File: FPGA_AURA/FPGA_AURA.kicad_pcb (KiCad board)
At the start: 10 copper layers, 50 x 50 mm, 161 parts, among them J1 SS5-40-3.00-X-D-K-XX, J2 SS5-20-3.00-X-D-K-XX, U1 XC7A35T-2FTG256C, U2 W25Q256JVEIQ, U200 ADP5014, U4 TPS51200DRCR, U500 MT41K128M16JT-125_IT_K

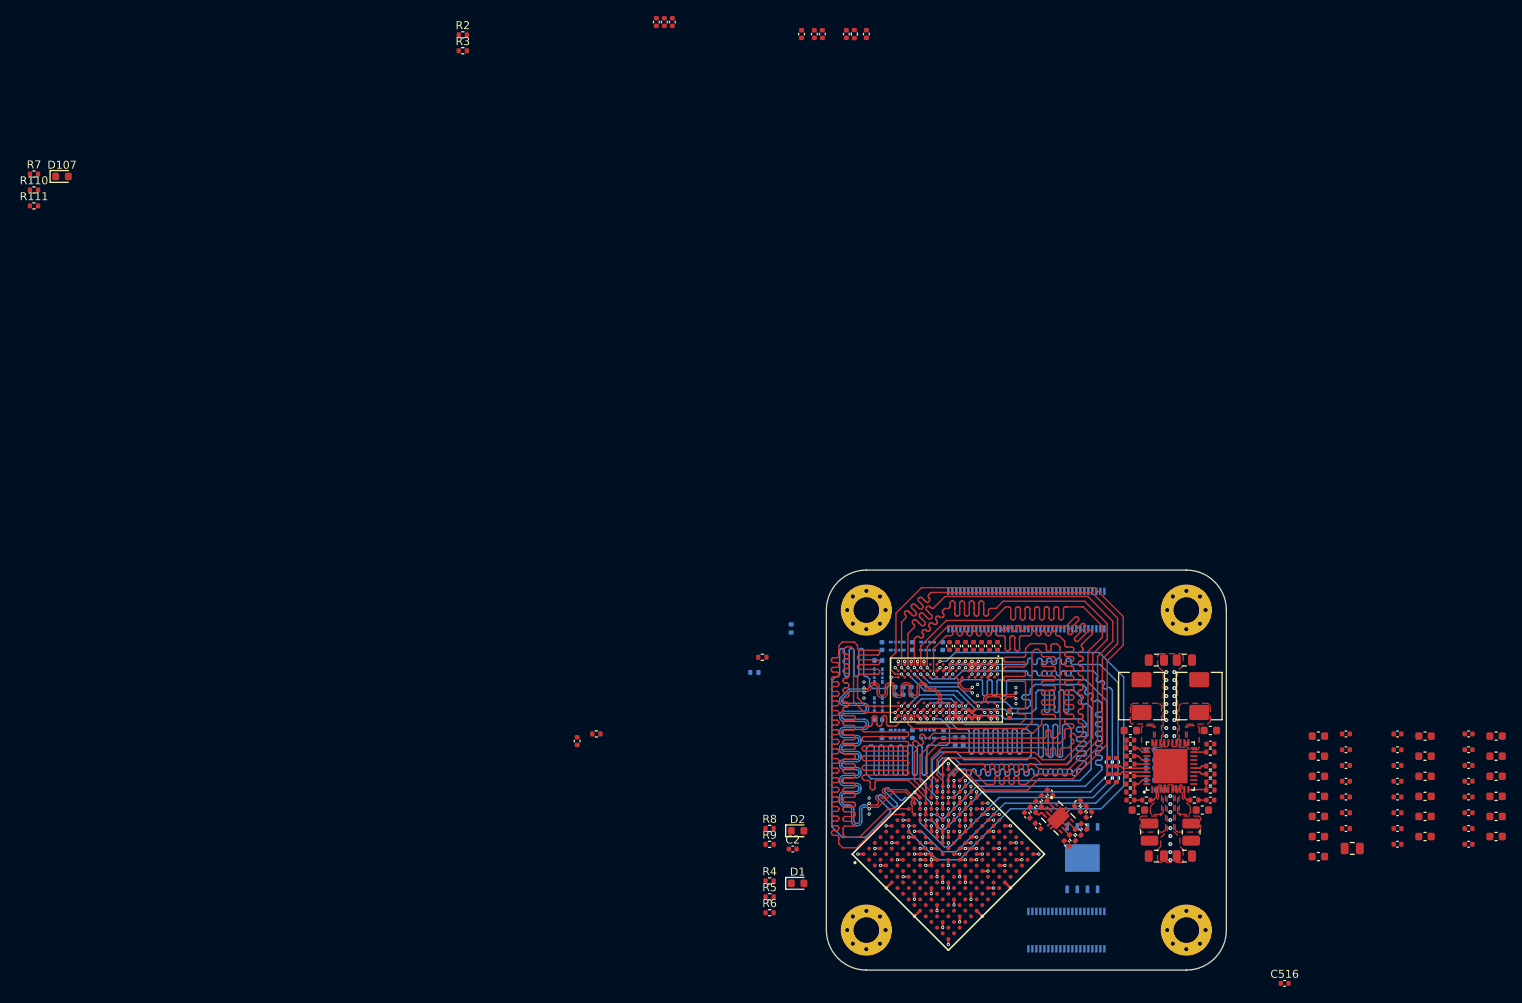
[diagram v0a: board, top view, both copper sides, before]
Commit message: Finished schematic to start routing again, and started MII fanout from connector.
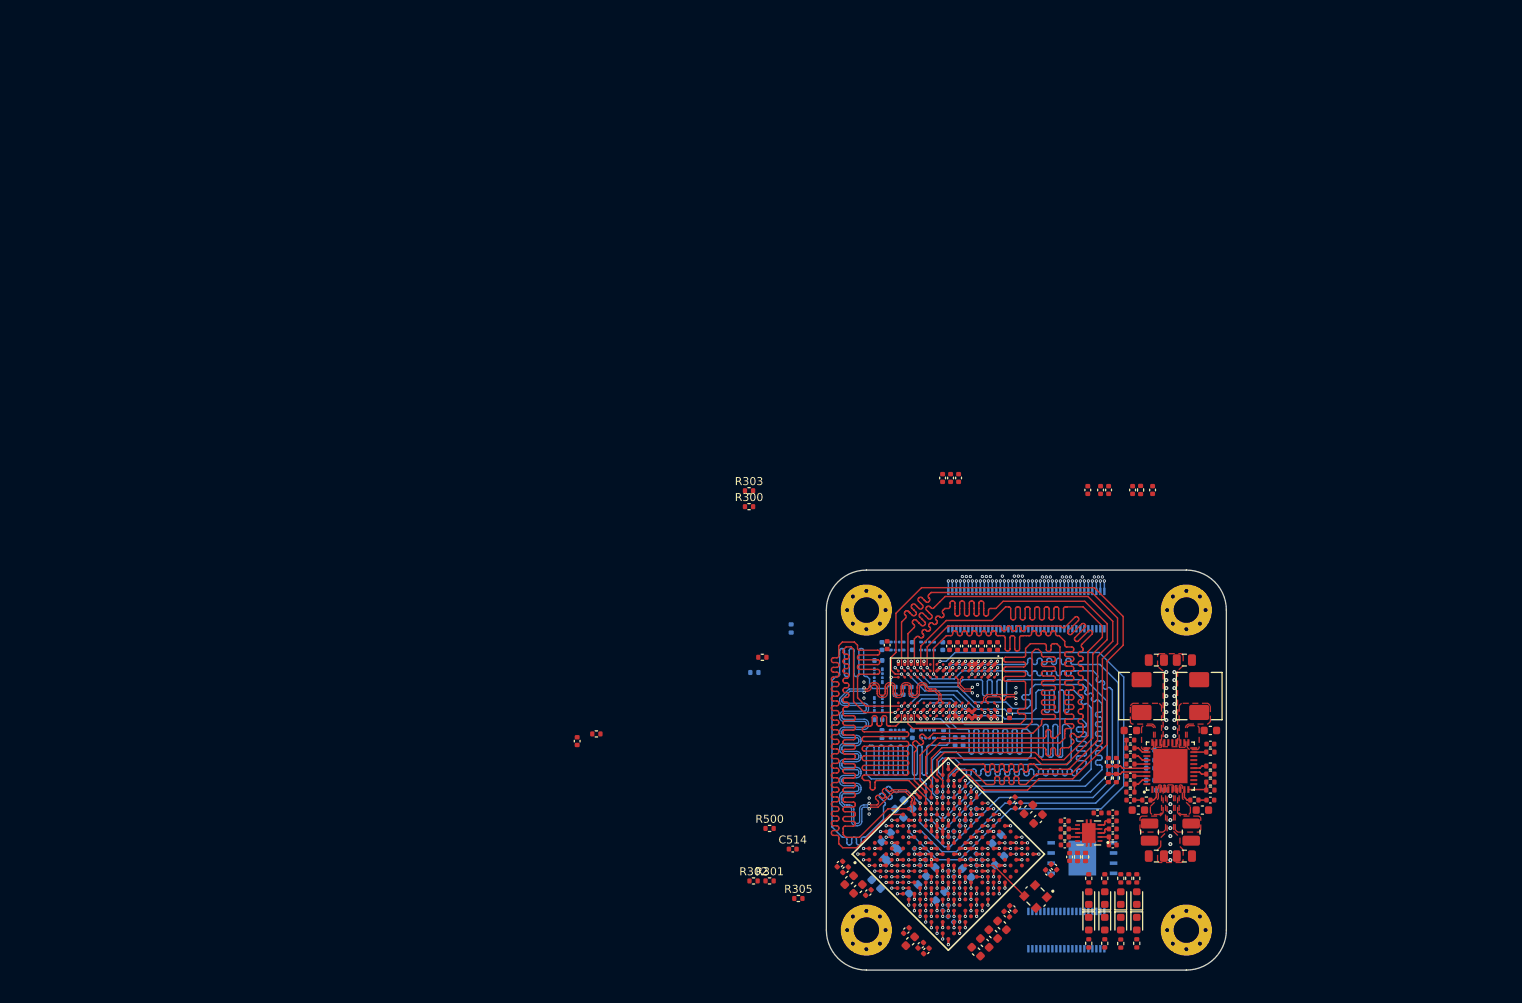
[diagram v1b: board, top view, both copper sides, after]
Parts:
- added D1: LED, LED_SMD:LED_0603_1608Metric, F.Cu at (138.8, 91.0)
- added D700: LED, LED_SMD:LED_0603_1608Metric, F.Cu at (132.8, 94.2)
- added D701: LED, LED_SMD:LED_0603_1608Metric, F.Cu at (134.8, 94.2)
- added D702: LED, LED_SMD:LED_0603_1608Metric, F.Cu at (136.8, 94.2)
- added D703: LED, LED_SMD:LED_0603_1608Metric, F.Cu at (138.8, 94.2)
- added R502: 470R, Resistor_SMD:R_0402_1005Metric, F.Cu at (138.8, 88.5)
- added R700: 27R, Resistor_SMD:R_0402_1005Metric, F.Cu at (132.8, 96.7)
- added R701: 120R, Resistor_SMD:R_0402_1005Metric, F.Cu at (134.8, 96.7)
- added R702: 80R, Resistor_SMD:R_0402_1005Metric, F.Cu at (136.8, 96.7)
- added R704: 470R, Resistor_SMD:R_0402_1005Metric, F.Cu at (138.8, 96.7)
- added Y500: ASEM1-100.000MHZ-LC-T, ASEM1-100.000MHZ-LC-T:XTAL_ASEM1-100.000MHZ-LC-T, F.Cu at (126.2, 90.8)
- C200: renamed from C32; moved to B.Cu
- C201: renamed from C18; moved to B.Cu
- C202: renamed from C19; moved to B.Cu
- C203: renamed from C20; moved to B.Cu
- C204: renamed from C27; moved to B.Cu
- C205: renamed from C26; moved to B.Cu
- C206: renamed from C23; moved to B.Cu
- C207: renamed from C21; moved to B.Cu
- C208: renamed from C28; moved to B.Cu
- C209: renamed from C25; moved to B.Cu
- C210: renamed from C22; moved to B.Cu
- C211: renamed from C24; moved to B.Cu
- C212: renamed from C29; moved to B.Cu
- C213: renamed from C30; moved to B.Cu
- C214: renamed from C31; moved to B.Cu
- C501: renamed from C46; moved to B.Cu
- C502: renamed from C45; moved to B.Cu
- C504: renamed from C42; moved to B.Cu
- C505: renamed from C41; moved to B.Cu
- C600: renamed from C33; value 47 -> 47u
- C605: renamed from C35; moved to B.Cu
- C607: renamed from C54; value 47 -> 47u
- C608: renamed from C57; moved to B.Cu
- C613: renamed from C58; moved to B.Cu
- J700: renamed from J1; value SS5-40-3.00-X-D-K-XX -> SS5-40-3.50-X-D-K-XX; footprint SS5-40-3.00-X-D-K-XX:SAMTEC_SS5-40-3.00-X-D-K-XX -> SS5-40-3.50-X-D-K-XX:SAMTEC_SS5-40-3.50-X-D-K-XX
- J701: renamed from J2; value SS5-20-3.00-X-D-K-XX -> SS5-20-3.50-X-D-K-XX; footprint SS5-20-3.00-X-D-K-XX:SAMTEC_SS5-20-3.00-X-D-K-XX -> SS5-20-3.50-X-D-K-XX:SAMTEC_SS5-20-3.50-X-D-K-XX
- moved R307 161.7 mm to (137.8, 88.5), turned to -90 degrees
- moved R306 160.2 mm to (134.8, 88.5), turned to -90 degrees
- moved D301 160.2 mm to (136.8, 91.0), turned to 90 degrees
- moved R308 159.7 mm to (136.8, 88.5), turned to 90 degrees
- moved C504 74.6 mm to (109.2, 79.3), turned to -135 degrees
- moved C600 74.2 mm to (102.8, 88.8), turned to -135 degrees
- moved C505 73.9 mm to (110.2, 80.4), turned to -135 degrees
- moved C606 72.8 mm to (104.0, 89.9), turned to -135 degrees
- moved C601 70.5 mm to (101.7, 86.8), turned to -135 degrees
- moved C602 70.2 mm to (102.4, 87.5), turned to -135 degrees
- moved C605 69.9 mm to (106.2, 89.3), turned to 135 degrees
- moved C603 68.5 mm to (105.2, 90.3), turned to -135 degrees
- moved C414 67.3 mm to (116.5, 38.5)
- moved C419 67.3 mm to (115.5, 38.5)
- moved C423 67.3 mm to (114.5, 38.5)
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- renumbered C200 to C100, C201 to C101, C202 to C102, C203 to C103, C205 to C105, C206 to C106, C207 to C107, C208 to C108, C209 to C109, C210 to C110, C211 to C111, C212 to C112, C213 to C113, C214 to C114, C215 to C115, C216 to C116, C217 to C117, C218 to C118, C219 to C119, C220 to C120, C221 to C121, C222 to C122, C1 to C300, C500 to C400, C501 to C401, C502 to C402, C503 to C403, C504 to C404, C505 to C405, C506 to C406, C507 to C407, C508 to C408, C510 to C410, C511 to C411, C512 to C412, C513 to C413, C514 to C414, C515 to C415, C516 to C416, C517 to C417, C518 to C418, C519 to C419, C520 to C420, C521 to C421, C522 to C422, C523 to C423, C524 to C424, C525 to C425, C526 to C426, C527 to C427, C528 to C428, C529 to C429, C530 to C430, C531 to C431, C43 to C500, C44 to C503, C40 to C506, C50 to C507, C51 to C508, C52 to C509, C53 to C510, C47 to C511, C48 to C512, C49 to C513, C2 to C514, C39 to C601, C38 to C602, C37 to C603, C36 to C604, C34 to C606, C56 to C609, C55 to C610, C60 to C611, C59 to C612, D1 to D300, D107 to D301, D2 to D500, L200 to L100, L201 to L101, L202 to L102, L203 to L103, R200 to R100, R201 to R101, R202 to R102, R203 to R103, R204 to R104, R205 to R105, R206 to R106, R207 to R107, R208 to R108, R209 to R109, R210 to R110, R211 to R111, R212 to R112, R213 to R113, R214 to R114, R215 to R115, R216 to R116, R217 to R117, R218 to R118, R219 to R119, R221 to R121, R222 to R122, R223 to R123, R3 to R300, R4 to R301, R5 to R302, R2 to R303, R1 to R304, R6 to R305, R7 to R306, R110 to R307, R111 to R308, R508 to R408, R509 to R409, R510 to R410, R511 to R411, R512 to R412, R513 to R413, R522 to R422, R523 to R423, R524 to R424, R525 to R425, R8 to R500, R9 to R501, U200 to U100
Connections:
- net /200_Power_Regulation/ADP_1V0_PD renamed /100_Power_Regulation/ADP_1V0_PD
- net /200_Power_Regulation/ADP_1V35_PD renamed /100_Power_Regulation/ADP_1V35_PD
- net /200_Power_Regulation/ADP_1V8_PD renamed /100_Power_Regulation/ADP_1V8_PD
- net /200_Power_Regulation/ADP_CFG1 renamed /100_Power_Regulation/ADP_CFG1
- net /200_Power_Regulation/ADP_CFG2 renamed /100_Power_Regulation/ADP_CFG2
- net /200_Power_Regulation/ADP_COMP1 renamed /100_Power_Regulation/ADP_COMP1
- net /200_Power_Regulation/ADP_COMP2 renamed /100_Power_Regulation/ADP_COMP2
- net /200_Power_Regulation/ADP_COMP3 renamed /100_Power_Regulation/ADP_COMP3
- net /200_Power_Regulation/ADP_COMP4 renamed /100_Power_Regulation/ADP_COMP4
- net /200_Power_Regulation/ADP_EN2 renamed /100_Power_Regulation/ADP_EN2
- net /200_Power_Regulation/ADP_EN4 renamed /100_Power_Regulation/ADP_EN4
- net /200_Power_Regulation/ADP_FB4 renamed /100_Power_Regulation/ADP_FB4
- net /200_Power_Regulation/ADP_RC1 renamed /100_Power_Regulation/ADP_RC1
- net /200_Power_Regulation/ADP_RC2 renamed /100_Power_Regulation/ADP_RC2
- net /200_Power_Regulation/ADP_RC3 renamed /100_Power_Regulation/ADP_RC3
- net /200_Power_Regulation/ADP_RC4 renamed /100_Power_Regulation/ADP_RC4
- net /200_Power_Regulation/ADP_RT renamed /100_Power_Regulation/ADP_RT
- net /200_Power_Regulation/ADP_SW1 renamed /100_Power_Regulation/ADP_SW1
- net /200_Power_Regulation/ADP_SW2 renamed /100_Power_Regulation/ADP_SW2
- net /200_Power_Regulation/ADP_SW3 renamed /100_Power_Regulation/ADP_SW3
- net /200_Power_Regulation/ADP_SW4 renamed /100_Power_Regulation/ADP_SW4
- net /200_Power_Regulation/ADP_UV renamed /100_Power_Regulation/ADP_UV
- net /200_Power_Regulation/TPS_REFIN renamed /100_Power_Regulation/TPS_REFIN
- net /400_FPGA_Config/DONE_0 renamed /300_FPGA_Config/DONE_0
- net /400_FPGA_Config/DONE_LED renamed /300_FPGA_Config/DONE_LED
- net /400_FPGA_Config/INIT_B_0 renamed /300_FPGA_Config/INIT_B_0
- net /400_FPGA_Config/INIT_LED renamed /300_FPGA_Config/INIT_LED
- net /400_FPGA_Config/M2_0 renamed /300_FPGA_Config/M2_0
- net /400_FPGA_Config/PROG_B renamed /300_FPGA_Config/PROG_B
- net /400_FPGA_Config/QSPI_CLK renamed /300_FPGA_Config/QSPI_CLK
- net /400_FPGA_Config/QSPI_CLK_R renamed /300_FPGA_Config/QSPI_CLK_R
- net /400_FPGA_Config/QSPI_CS# renamed /300_FPGA_Config/QSPI_CS#
- net /400_FPGA_Config/QSPI_IO0 renamed /300_FPGA_Config/QSPI_IO0
- net /400_FPGA_Config/QSPI_IO1 renamed /300_FPGA_Config/QSPI_IO1
- net /400_FPGA_Config/QSPI_IO2 renamed /300_FPGA_Config/QSPI_IO2
- net /400_FPGA_Config/QSPI_IO3 renamed /300_FPGA_Config/QSPI_IO3
- net /500_DDR3L/DDR3_ZQ renamed /400_DDR3L/DDR3_ZQ
- net /600_FPGA_Banks_14_15/INIT_CALIB renamed /500_FPGA_Banks_14_15/INIT_CALIB
- net /600_FPGA_Banks_14_15/INIT_CALIB_LED renamed /500_FPGA_Banks_14_15/INIT_CALIB_LED
- U1 pad K13: unconnected-(U1C-IO_L5P_T0_D06_14-PadK13) -> /500_FPGA_Banks_14_15/GPIO
- U1 pad N11: /600_FPGA_Banks_14_15/100MHZ_CLK -> /500_FPGA_Banks_14_15/100MHZ_CLK
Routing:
- net ETH_1_TXD_3: track 0.00 -> 56.6 mm, vias 0 -> 2
- net ETH_1_TXD_2: track 0.00 -> 56.1 mm, vias 0 -> 2
- net ETH_1_TXD_1: track 0.00 -> 55.5 mm, vias 0 -> 2
- net ETH_1_TXD_0: track 0.00 -> 54.9 mm, vias 0 -> 2
- net ETH_1_TX_EN: track 0.00 -> 54.6 mm, vias 0 -> 2
- net ETH_1_TX_CLK: track 0.00 -> 53.9 mm, vias 0 -> 2
- net ETH_1_RXD_3: track 0.00 -> 53.6 mm, vias 0 -> 2
- net ETH_1_RXD_2: track 0.00 -> 53.0 mm, vias 0 -> 2
- net ETH_1_RXD_1: track 0.00 -> 52.3 mm, vias 0 -> 2
- net ETH_1_RXD_0: track 0.00 -> 51.6 mm, vias 0 -> 2
- net ETH_1_COL: track 0.00 -> 51.2 mm, vias 0 -> 2
- net ETH_1_RX_ER: track 0.00 -> 50.5 mm, vias 0 -> 2
- net ETH_1_CRS: track 0.00 -> 49.9 mm, vias 0 -> 2
- net ETH_1_RX_DV: track 0.00 -> 49.2 mm, vias 0 -> 2
- net ETH_1_RX_CLK: track 0.00 -> 48.8 mm, vias 0 -> 2
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- added copper zone on F.Cu, net (none)
- added copper zone on In4.Cu, net GND
- added copper zone on In6.Cu, net GND
- added copper zone on In8.Cu, net GND
- removed copper zone on F.Cu, net /100_Power_Regulation/ADP_SW1
- removed copper zone on F.Cu, net /100_Power_Regulation/ADP_SW2
- removed copper zone on F.Cu, net /100_Power_Regulation/ADP_SW3
- removed copper zone on F.Cu, net /100_Power_Regulation/ADP_SW4

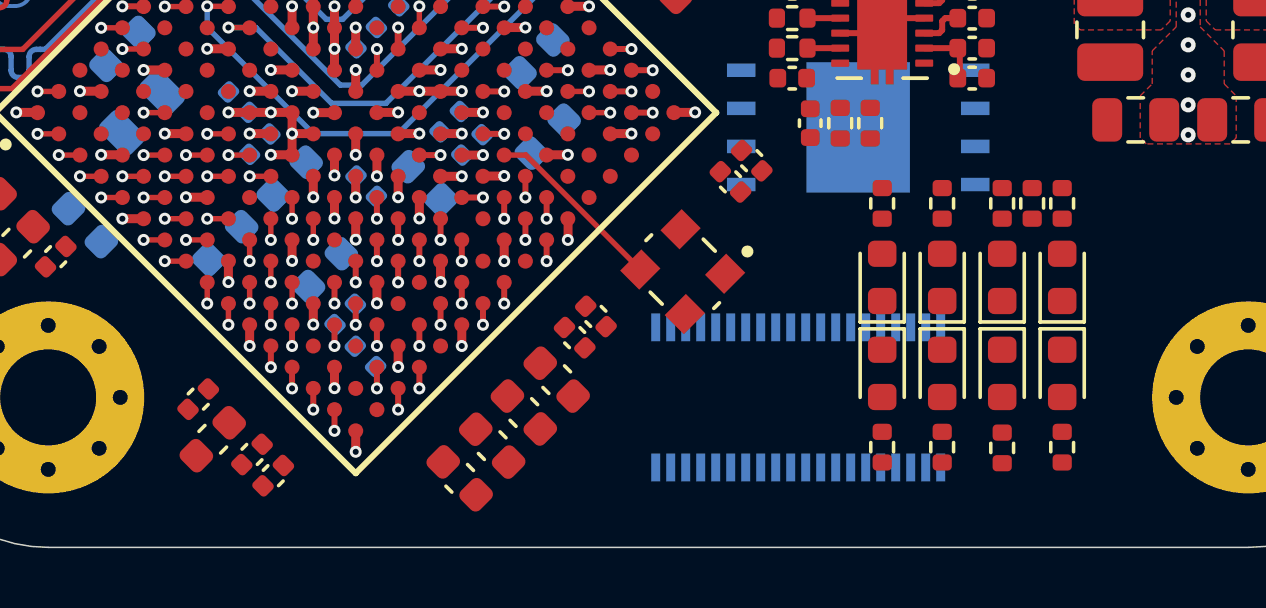
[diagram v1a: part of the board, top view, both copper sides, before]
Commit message: MII FPGA Breakout complete, pin reasignment TODO, and other peripherals
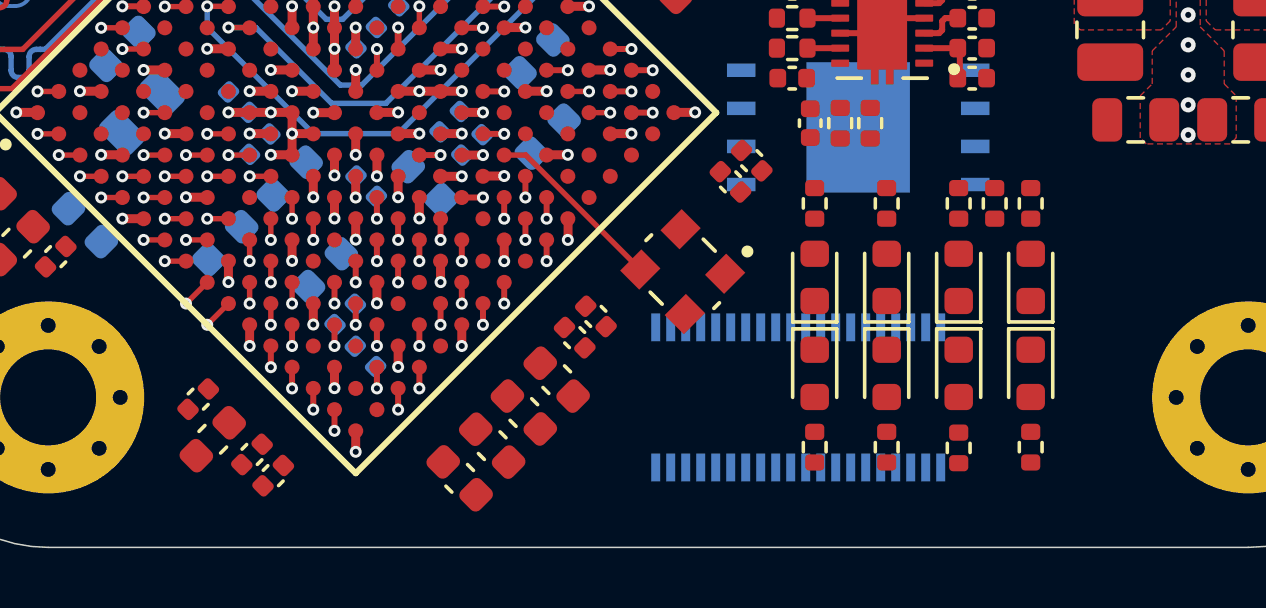
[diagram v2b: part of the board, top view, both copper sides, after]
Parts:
- moved D500 2.25 mm to (130.5, 91.0)
- moved D700 2.25 mm to (130.6, 94.2)
- moved R501 2.25 mm to (130.5, 88.5)
- moved R700 2.25 mm to (130.6, 96.7)
- moved D300 1.85 mm to (132.9, 91.0)
- moved D701 1.85 mm to (132.9, 94.2)
- moved R306 1.85 mm to (132.9, 88.5)
- moved R701 1.85 mm to (132.9, 96.7)
- moved D301 1.45 mm to (135.3, 91.0)
- moved D702 1.45 mm to (135.3, 94.2)
- moved R308 1.45 mm to (135.4, 88.5)
- moved R702 1.45 mm to (135.3, 96.7)
- moved R307 1.25 mm to (136.6, 88.5)
- moved D1 1.05 mm to (137.8, 91.0)
- moved D703 1.05 mm to (137.8, 94.2)
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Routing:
- net ETH_0_TX_CLK: track 46.1 -> 79.2 mm
- net ETH_0_RXD_1: track 45.5 -> 74.0 mm
- net ETH_0_RXD_0: track 45.2 -> 73.6 mm
- net ETH_0_RXD_3: track 46.0 -> 74.4 mm
- net ETH_1_TX_CLK: track 53.9 -> 79.4 mm
- net ETH_0_RX_DV: track 44.2 -> 68.6 mm
- net ETH_0_RX_CLK: track 44.1 -> 67.1 mm
- net ETH_0_RX_ER: track 44.8 -> 67.3 mm
- net ETH_1_TX_EN: track 54.6 -> 76.8 mm
- net ETH_1_RX_CLK: track 48.8 -> 69.9 mm
- net ETH_0_TXD_2: track 47.1 -> 67.3 mm
- net ETH_0_TXD_3: track 47.4 -> 67.6 mm
- net ETH_0_RXD_2: track 45.7 -> 65.5 mm
- net ETH_1_TXD_1: track 55.5 -> 75.1 mm
- net ETH_0_TXD_1: track 46.8 -> 65.1 mm
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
